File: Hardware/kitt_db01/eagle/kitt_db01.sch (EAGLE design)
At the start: 94 parts, among them U1 ADNS-3080, U2 MIC5205-3.3YM5TR, U9.01 SI1922EDH, X1 RESON

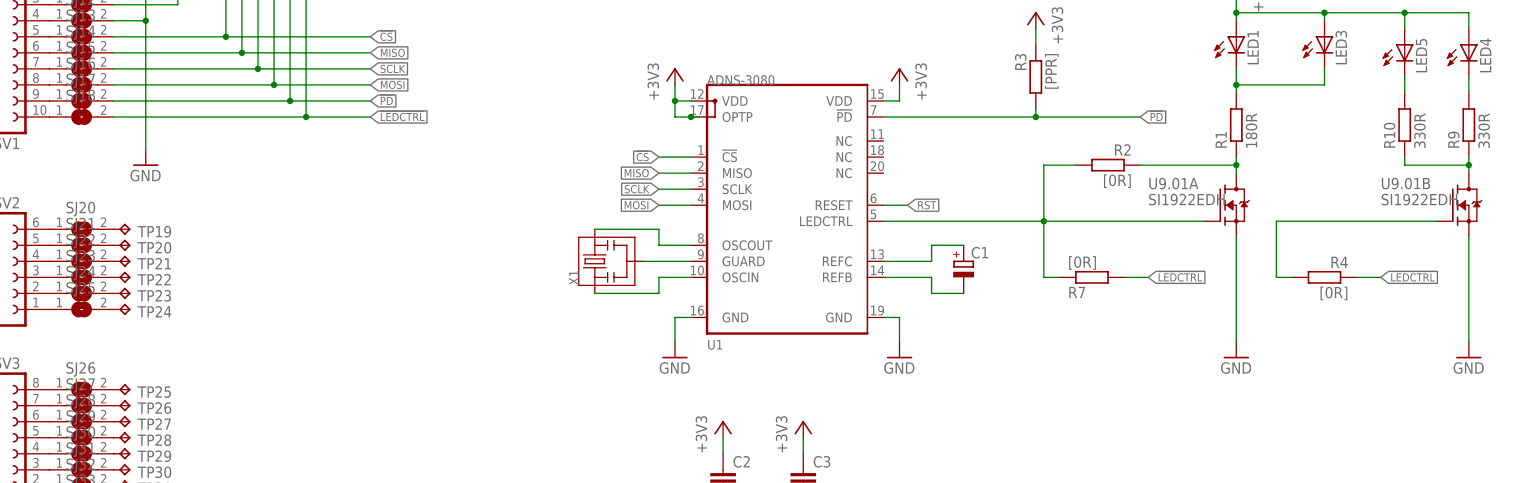
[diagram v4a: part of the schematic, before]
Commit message: snapshot of db01 board layout : almost done edition -> now exporting BOM for this design -> footprints are all go -> powerplane and grounding to be done after BOM
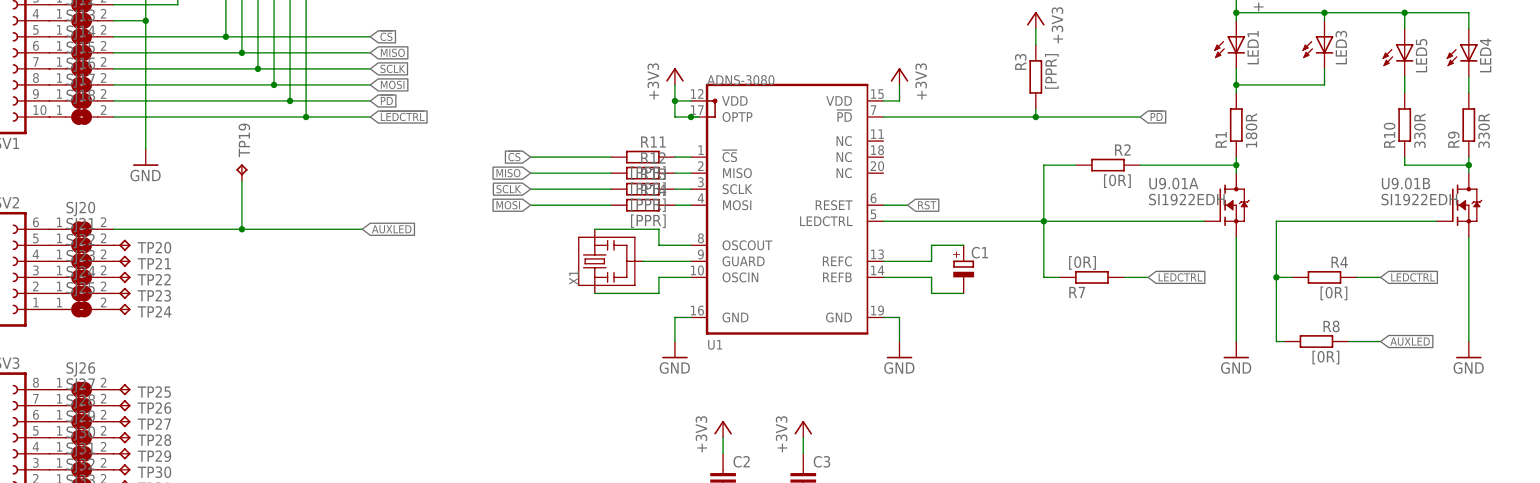
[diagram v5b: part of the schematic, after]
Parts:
- added R11, R12, R13, R14: [PPR], rcl:R-EU_R0805
- added R8: [0R], rcl:R-EU_R0805
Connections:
- new net AUXLED: R8.1, SJ20.2, TP19.TP
- new net N$182: R12.1, U1.MISO
- new net N$183: R13.1, U1.SCLK
- new net N$188: R14.1, U1.MOSI
- net !CS: now also R11.2; no longer U1.!CS
- net MISO: now also R12.2; no longer U1.MISO
- net MOSI: now also R14.2; no longer U1.MOSI
- net N$168: now also R11.1, U1.!CS; no longer SJ20.2, TP19.TP
- net N$184: now also R8.2
- net SCLK: now also R13.2; no longer U1.SCLK
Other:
- moved on the sheet: TP19
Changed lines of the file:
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@@
 <part name="LED5" library="led" deviceset="LED" device="CHIP-LED0805"/>
 <part name="R10" library="rcl" deviceset="R-EU_" device="R0805" value="330R"/>
+<part name="R8" library="rcl" deviceset="R-EU_" device="R0805" value="[0R]"/>
+<part name="R11" library="rcl" deviceset="R-EU_" device="R0805" value="[PPR]"/>
+<part name="R12" library="rcl" deviceset="R-EU_" device="R0805" value="[PPR]"/>
+<part name="R13" library="rcl" deviceset="R-EU_" device="R0805" value="[PPR]"/>
+<part name="R14" library="rcl" deviceset="R-EU_" device="R0805" value="[PPR]"/>
 </parts>
 <sheets>
@@
 <instance part="SJ32" gate="1" x="27.94" y="43.18"/>
 <instance part="SJ33" gate="1" x="27.94" y="40.64"/>
-<instance part="TP19" gate="G$1" x="35.56" y="83.82" smashed="yes" rot="R270">
-<attribute name="NAME" x="36.83" y="82.55" size="1.778" layer="95"/>
-<attribute name="TP_SIGNAL_NAME" x="34.29" y="82.55" size="1.778" layer="97" rot="R270"/>
+<instance part="TP19" gate="G$1" x="53.34" y="93.98" smashed="yes">
+<attribute name="NAME" x="54.61" y="95.25" size="1.778" layer="95" rot="R90"/>
+<attribute name="TP_SIGNAL_NAME" x="54.61" y="92.71" size="1.778" layer="97"/>
 </instance>
 <instance part="TP20" gate="G$1" x="35.56" y="81.28" smashed="yes" rot="R270">
@@
 <instance part="LED5" gate="G$1" x="237.49" y="113.03"/>
 <instance part="R10" gate="G$1" x="237.49" y="100.33" rot="R90"/>
+<instance part="R8" gate="G$1" x="223.52" y="66.04" rot="MR0"/>
+<instance part="R11" gate="G$1" x="116.84" y="95.25" rot="MR0"/>
+<instance part="R12" gate="G$1" x="116.84" y="92.71" rot="MR0"/>
+<instance part="R13" gate="G$1" x="116.84" y="90.17" rot="MR0"/>
+<instance part="R14" gate="G$1" x="116.84" y="87.63" rot="MR0"/>
 </instances>
 <busses>
@@
 <net name="MOSI" class="0">
 <segment>
-<wire x1="124.46" y1="87.63" x2="119.38" y2="87.63" width="0.1524" layer="91"/>
-<label x="119.38" y="87.63" size="1.27" layer="95" font="vector" rot="R180" xref="yes"/>
-<pinref part="U1" gate="G$1" pin="MOSI"/>
+<label x="99.06" y="87.63" size="1.27" layer="95" font="vector" rot="R180" xref="yes"/>
+<wire x1="111.76" y1="87.63" x2="99.06" y2="87.63" width="0.1524" layer="91"/>
+<pinref part="R14" gate="G$1" pin="2"/>
 </segment>
 <segment>
@@
 <net name="MISO" class="0">
 <segment>
-<wire x1="124.46" y1="92.71" x2="119.38" y2="92.71" width="0.1524" layer="91"/>
-<label x="119.38" y="92.71" size="1.27" layer="95" font="vector" rot="R180" xref="yes"/>
-<pinref part="U1" gate="G$1" pin="MISO"/>
+<label x="99.06" y="92.71" size="1.27" layer="95" font="vector" rot="R180" xref="yes"/>
+<wire x1="111.76" y1="92.71" x2="99.06" y2="92.71" width="0.1524" layer="91"/>
+<pinref part="R12" gate="G$1" pin="2"/>
 </segment>
 <segment>
@@
 <net name="!CS" class="0">
 <segment>
-<wire x1="124.46" y1="95.25" x2="119.38" y2="95.25" width="0.1524" layer="91"/>
-<label x="119.38" y="95.25" size="1.27" layer="95" font="vector" rot="R180" xref="yes"/>
-<pinref part="U1" gate="G$1" pin="!CS"/>
+<label x="99.06" y="95.25" size="1.27" layer="95" font="vector" rot="R180" xref="yes"/>
+<wire x1="111.76" y1="95.25" x2="99.06" y2="95.25" width="0.1524" layer="91"/>
+<pinref part="R11" gate="G$1" pin="2"/>
 </segment>
 <segment>
@@
 <net name="SCLK" class="0">
 <segment>
-<wire x1="124.46" y1="90.17" x2="119.38" y2="90.17" width="0.1524" layer="91"/>
-<label x="119.38" y="90.17" size="1.27" layer="95" font="vector" rot="R180" xref="yes"/>
-<pinref part="U1" gate="G$1" pin="SCLK"/>
+<label x="99.06" y="90.17" size="1.27" layer="95" font="vector" rot="R180" xref="yes"/>
+<wire x1="111.76" y1="90.17" x2="99.06" y2="90.17" width="0.1524" layer="91"/>
+<pinref part="R13" gate="G$1" pin="2"/>
 </segment>
 <segment>
@@
 </segment>
 </net>
-<net name="N$168" class="0">
+<net name="AUXLED" class="0">
 <segment>
 <pinref part="SJ20" gate="1" pin="2"/>
 <pinref part="TP19" gate="G$1" pin="TP"/>
+<wire x1="53.34" y1="91.44" x2="53.34" y2="83.82" width="0.1524" layer="91"/>
+<wire x1="53.34" y1="83.82" x2="33.02" y2="83.82" width="0.1524" layer="91"/>
+<wire x1="53.34" y1="83.82" x2="72.39" y2="83.82" width="0.1524" layer="91"/>
+<junction x="53.34" y="83.82"/>
+<label x="72.39" y="83.82" size="1.27" layer="95" xref="yes"/>
+</segment>
+<segment>
+<wire x1="228.6" y1="66.04" x2="233.68" y2="66.04" width="0.1524" layer="91"/>
+<pinref part="R8" gate="G$1" pin="1"/>
+<label x="233.68" y="66.04" size="1.27" layer="95" xref="yes"/>
 </segment>
 </net>
@@
 <wire x1="217.17" y1="76.2" x2="217.17" y2="85.09" width="0.1524" layer="91"/>
 <wire x1="217.17" y1="85.09" x2="242.57" y2="85.09" width="0.1524" layer="91"/>
+<pinref part="R8" gate="G$1" pin="2"/>
+<wire x1="218.44" y1="66.04" x2="217.17" y2="66.04" width="0.1524" layer="91"/>
+<wire x1="217.17" y1="66.04" x2="217.17" y2="76.2" width="0.1524" layer="91"/>
+<junction x="217.17" y="76.2"/>
 </segment>
 </net>
@@
 </segment>
 </net>
+<net name="N$168" class="0">
+<segment>
+<pinref part="R11" gate="G$1" pin="1"/>
+<pinref part="U1" gate="G$1" pin="!CS"/>
+<wire x1="121.92" y1="95.25" x2="124.46" y2="95.25" width="0.1524" layer="91"/>
+</segment>
+</net>
+<net name="N$182" class="0">
+<segment>
+<pinref part="R12" gate="G$1" pin="1"/>
+<pinref part="U1" gate="G$1" pin="MISO"/>
+<wire x1="121.92" y1="92.71" x2="124.46" y2="92.71" width="0.1524" layer="91"/>
+</segment>
+</net>
+<net name="N$183" class="0">
+<segment>
+<pinref part="R13" gate="G$1" pin="1"/>
+<pinref part="U1" gate="G$1" pin="SCLK"/>
+<wire x1="121.92" y1="90.17" x2="124.46" y2="90.17" width="0.1524" layer="91"/>
+</segment>
+</net>
+<net name="N$188" class="0">
+<segment>
+<pinref part="R14" gate="G$1" pin="1"/>
+<pinref part="U1" gate="G$1" pin="MOSI"/>
+<wire x1="121.92" y1="87.63" x2="124.46" y2="87.63" width="0.1524" layer="91"/>
+</segment>
+</net>

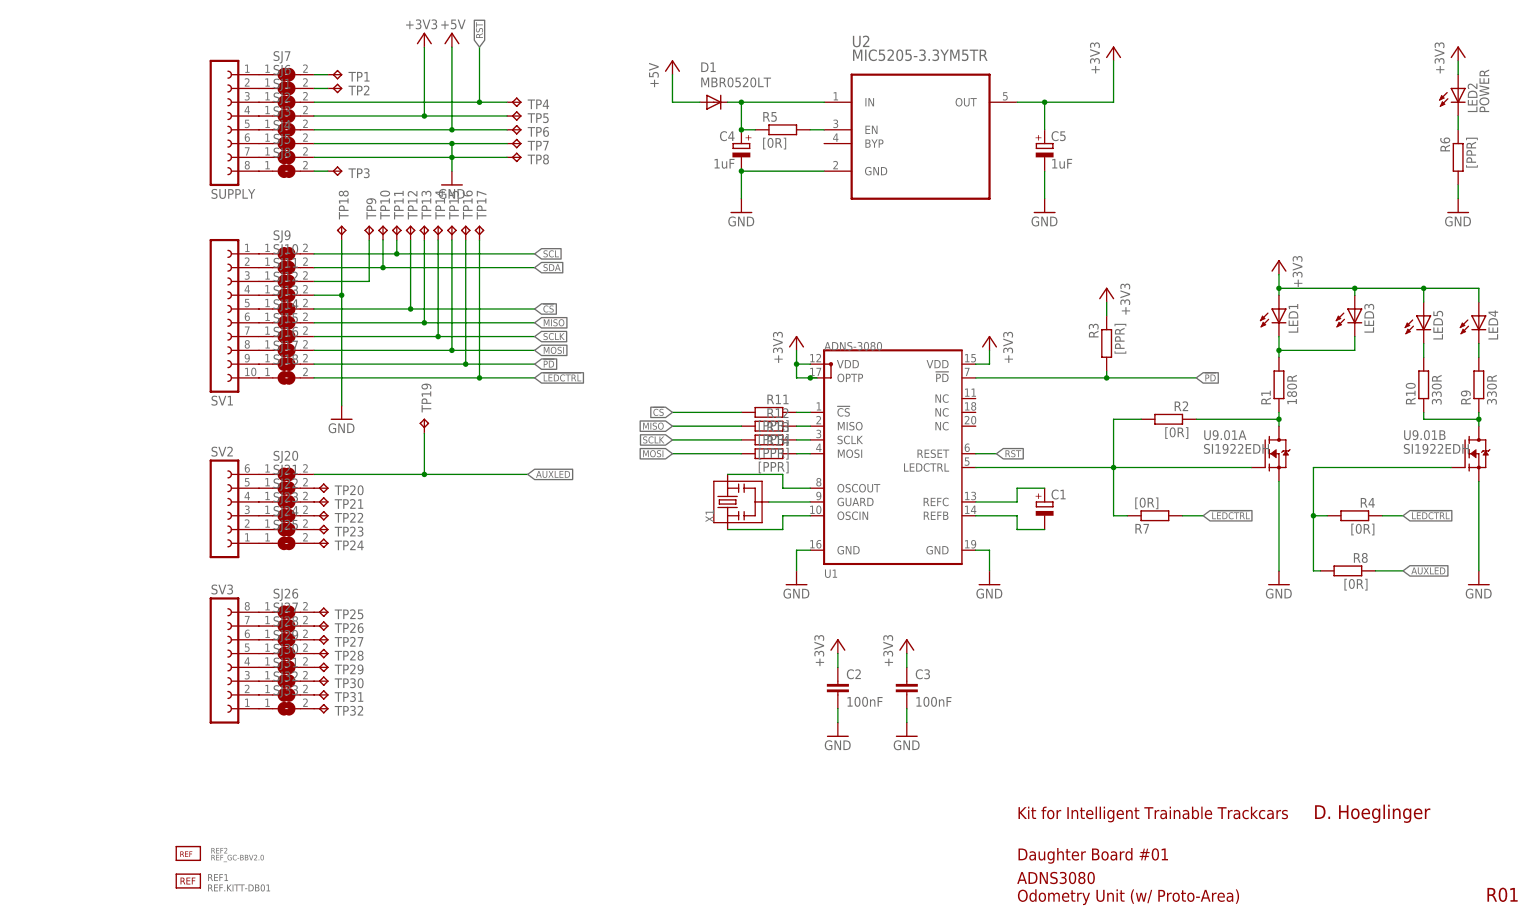
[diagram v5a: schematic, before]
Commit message: finished part search for db-01, updated footprints accordingly
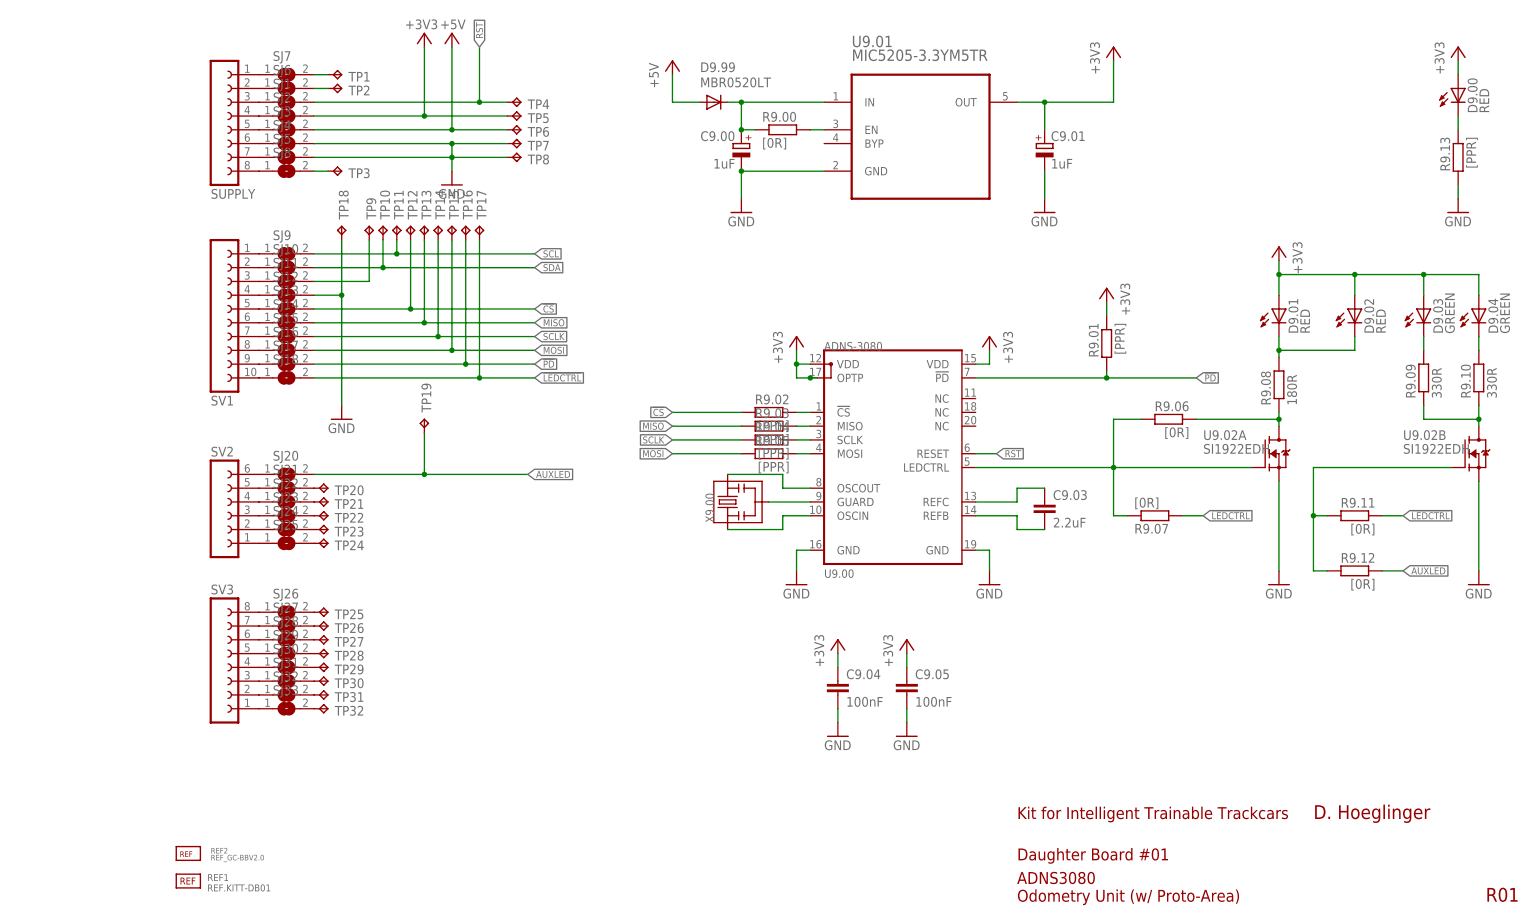
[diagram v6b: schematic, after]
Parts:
- removed C1: (no value), rcl:CPOL-EUSMCB
- removed LED4, LED5: (no value), led:LEDCHIP-LED0805
- removed R10, R9: 330R, rcl:R-EU_R0805
- removed R8: [0R], rcl:R-EU_R0805
- removed U2: MIC5205-3.3YM5TR, kitt.ic:MIC5205-3.3YM5TR
- added C9.03: 2.2uF, rcl:C-EUC1608
- added D9.03, D9.04: GREEN, led:LEDCHIP-LED0805
- added R9.09, R9.10: 330R, rcl:R-EU_R0805
- added R9.12: [0R], rcl:R-EU_R0805
- added U9.02: SI1922EDH, kitt.ic:SI1922EDH
- D9.00: value POWER -> RED
- D9.01, D9.02: value (none) -> RED
- U9.01: value SI1922EDH -> MIC5205-3.3YM5TR; device kitt.ic:SI1922EDH -> kitt.ic:MIC5205-3.3YM5TR
- renumbered C2 to C9.04, C3 to C9.05, C4 to C9.00, C5 to C9.01, D1 to D9.99, LED1 to D9.01, LED2 to D9.00, LED3 to D9.02, R1 to R9.08, R11 to R9.02, R12 to R9.03, R13 to R9.04, R14 to R9.05, R2 to R9.06, R3 to R9.01, R4 to R9.11, R5 to R9.00, R6 to R9.13, R7 to R9.07, U1 to U9.00, X1 to X9.00
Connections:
- net +3V3: now also D9.03.A, D9.04.A, U9.01.OUT; no longer LED4.A, LED5.A, U2.OUT
- net AUXLED: now also R9.12.1; no longer R8.1
- net GND: now also U9.01.GND, U9.02A.S, U9.02B.S; no longer U2.GND, U9.01A.S, U9.01B.S
- net N$10: now also U9.01.EN; no longer U2.EN
- net N$184: now also R9.12.2, U9.02B.G; no longer R8.2, U9.01B.G
- net N$185: now also D9.04.C, R9.10.2; no longer LED4.C, R9.2
- net N$186: now also R9.09.1, R9.10.1, U9.02B.D; no longer R10.1, R9.1, U9.01B.D
- net N$187: now also D9.03.C, R9.09.2; no longer LED5.C, R10.2
- net N$4: now also U9.02A.G; no longer U9.01A.G
- net N$5: now also C9.03.1; no longer C1.+
- net N$6: now also C9.03.2; no longer C1.-
- net N$7: now also U9.02A.D; no longer U9.01A.D
- net N$9: now also U9.01.IN; no longer U2.IN
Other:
- note added: "todo: clean up"
